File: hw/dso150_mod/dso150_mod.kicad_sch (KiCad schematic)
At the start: 23 parts, among them J1 USB_C_Receptacle_USB2.0, J2 Conn_01x02, J3 Conn_01x02, J4 Conn_01x04, J5 Conn_01x02, J6 Conn_01x01, SW1 SW_SPDT, U1 AP3012, U2 MCP73832-2-OT

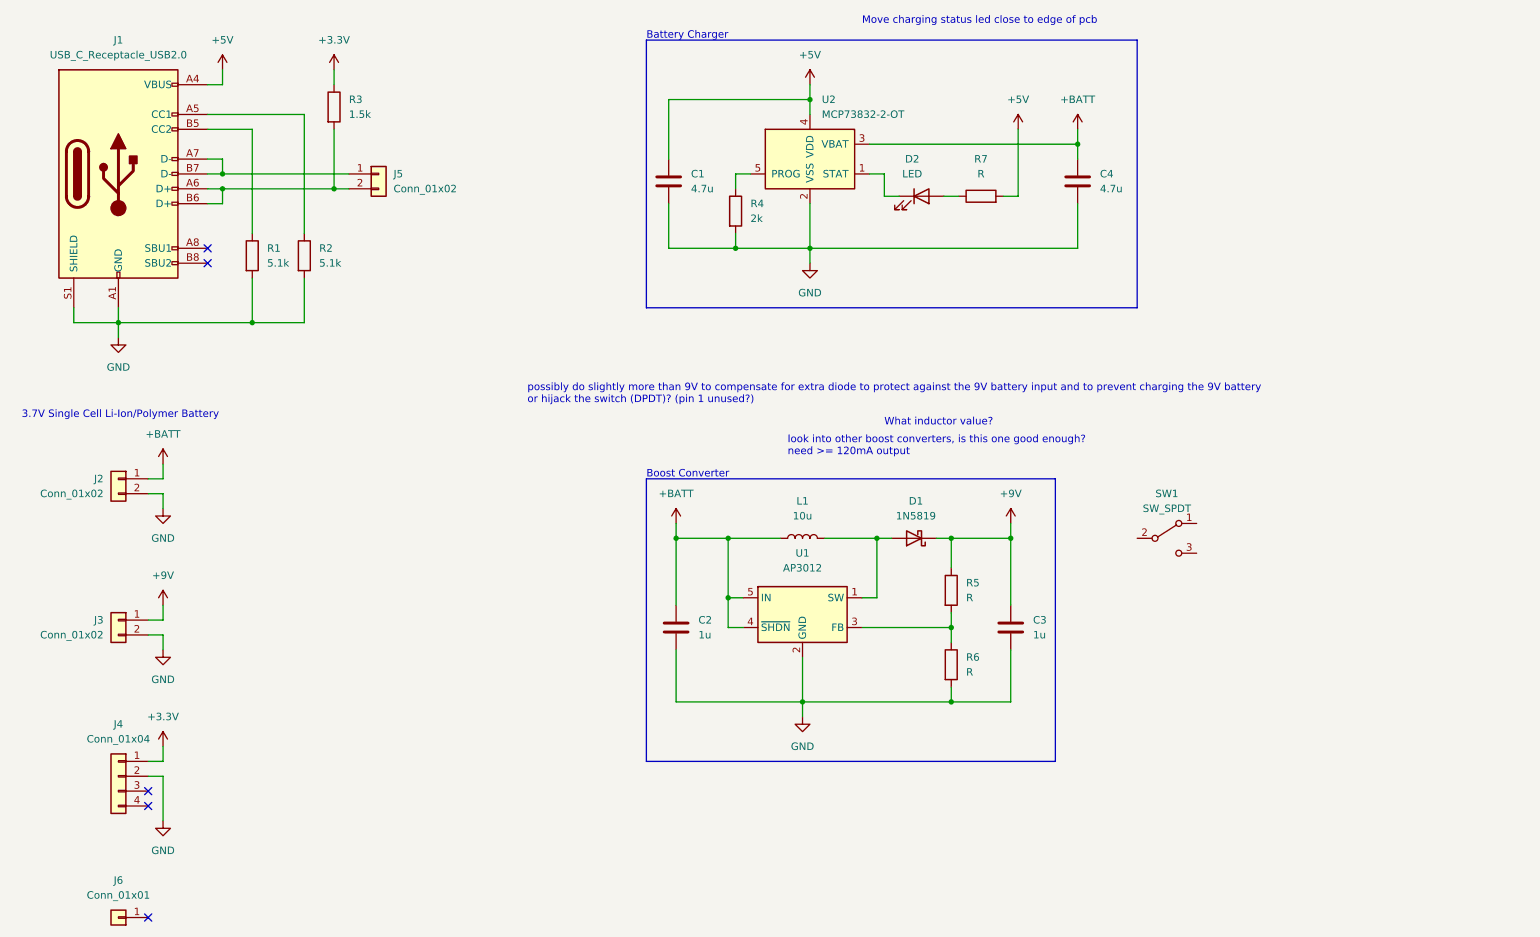
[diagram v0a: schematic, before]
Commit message: More layout placement, start traces
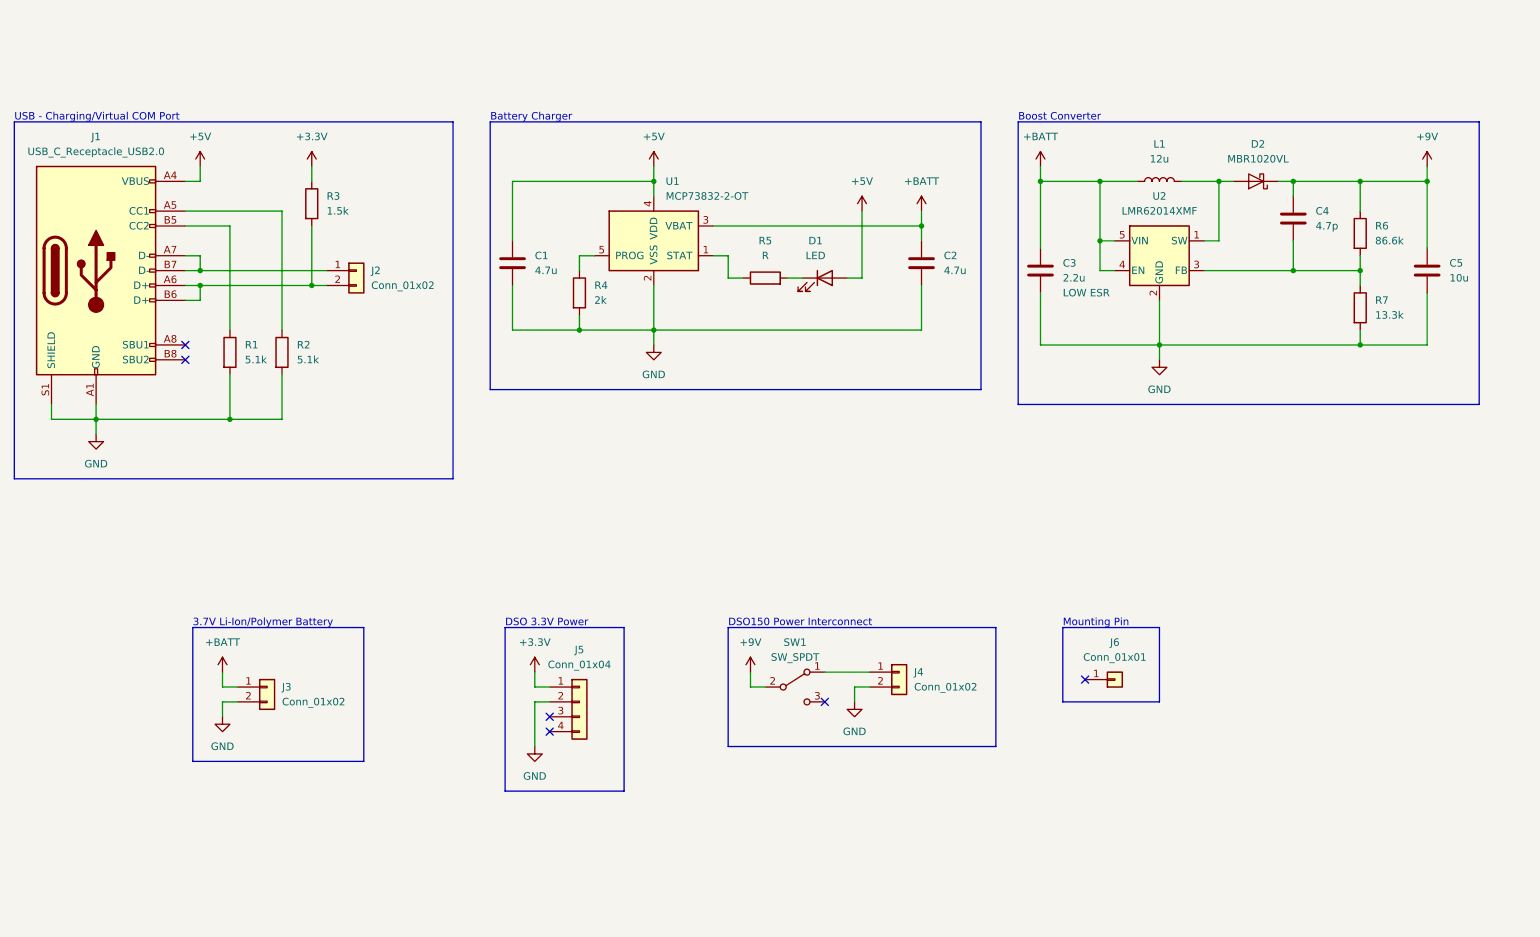
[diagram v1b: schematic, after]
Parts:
- removed D1: 1N5819, Diode_SMD:D_SOD-123F, symbol Device:D_Schottky
- removed U1: AP3012, Package_TO_SOT_SMD:SOT-23-5, symbol Regulator_Switching:AP3012
- added C4: 4.7p, Capacitor_SMD:C_0603_1608Metric, symbol Device:C
- added D2: MBR1020VL, Diode_SMD:D_SOD-123F, symbol Diode:MBR1020VL
- added U2: LMR62014XMF, Package_TO_SOT_SMD:SOT-23-5, symbol Regulator_Switching:LMR62014XMF
- C3: renamed from C2; value 1u -> 2.2u; Note (none) -> LOW ESR
- C5: renamed from C3; value 1u -> 10u
- L1: value 10u -> 12u; footprint Inductor_SMD:L_Bourns_SRN6045TA -> dso150_mod:L_Bourns_SRR0745A
- R6: renamed from R5; value R -> 86.6k
- R7: renamed from R6; value R -> 13.3k
- renumbered C4 to C2, D2 to D1, J5 to J2, J2 to J3, J3 to J4, J4 to J5, R7 to R5, U2 to U1
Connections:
- net +5V: now also D1.2 (A); no longer R5.2
- net +9V: now also SW1.2 (B), C4.1, D2.1 (K); no longer J4.1 (Pin_1)
- net +BATT: now also U2.4 (EN), U2.5 (VIN)
- net GND: now also U2.2 (GND)
- net at L1.2: now also D2.2 (A), U2.1 (SW)
- net at R6.2, R7.1: now also C4.2, U2.3 (FB)
- net at R5.1: now also U1.1 (STAT); no longer D1.2 (A)
- net at SW1.1 (A): now also J4.1 (Pin_1)
- net at D1.1 (K): now also R5.2; no longer U1.1 (STAT)
- no-connect marks 5 -> 6
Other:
- note added: "3.7V Li-Ion/Polymer Battery"
- note added: "DSO 3.3V Power"
- note added: "DSO150 Power Interconnect"
- note added: "Mounting Pin"
- note added: "USB - Charging/Virtual COM Port"
- note removed: "3.7V Single Cell Li-Ion/Polymer Battery"
- note removed: "Move charging status led close to edge of pcb"
- note removed: "What inductor value?"
- note removed: "look into other boost converters, is this one good enough? need >= 120mA output"
- note removed: "possibly do slightly more than 9V to compensate for extra diode to protect against the 9V battery input and to prevent charging the 9V battery or hijack the switch (DPDT)? (pin 1 unused?)"
- moved on the sheet: C1, C2, C3, C5, D1, J1, J2, J3, J4, J5, J6, L1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

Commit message: Disable boost converter to conserve battery, first final layout complete
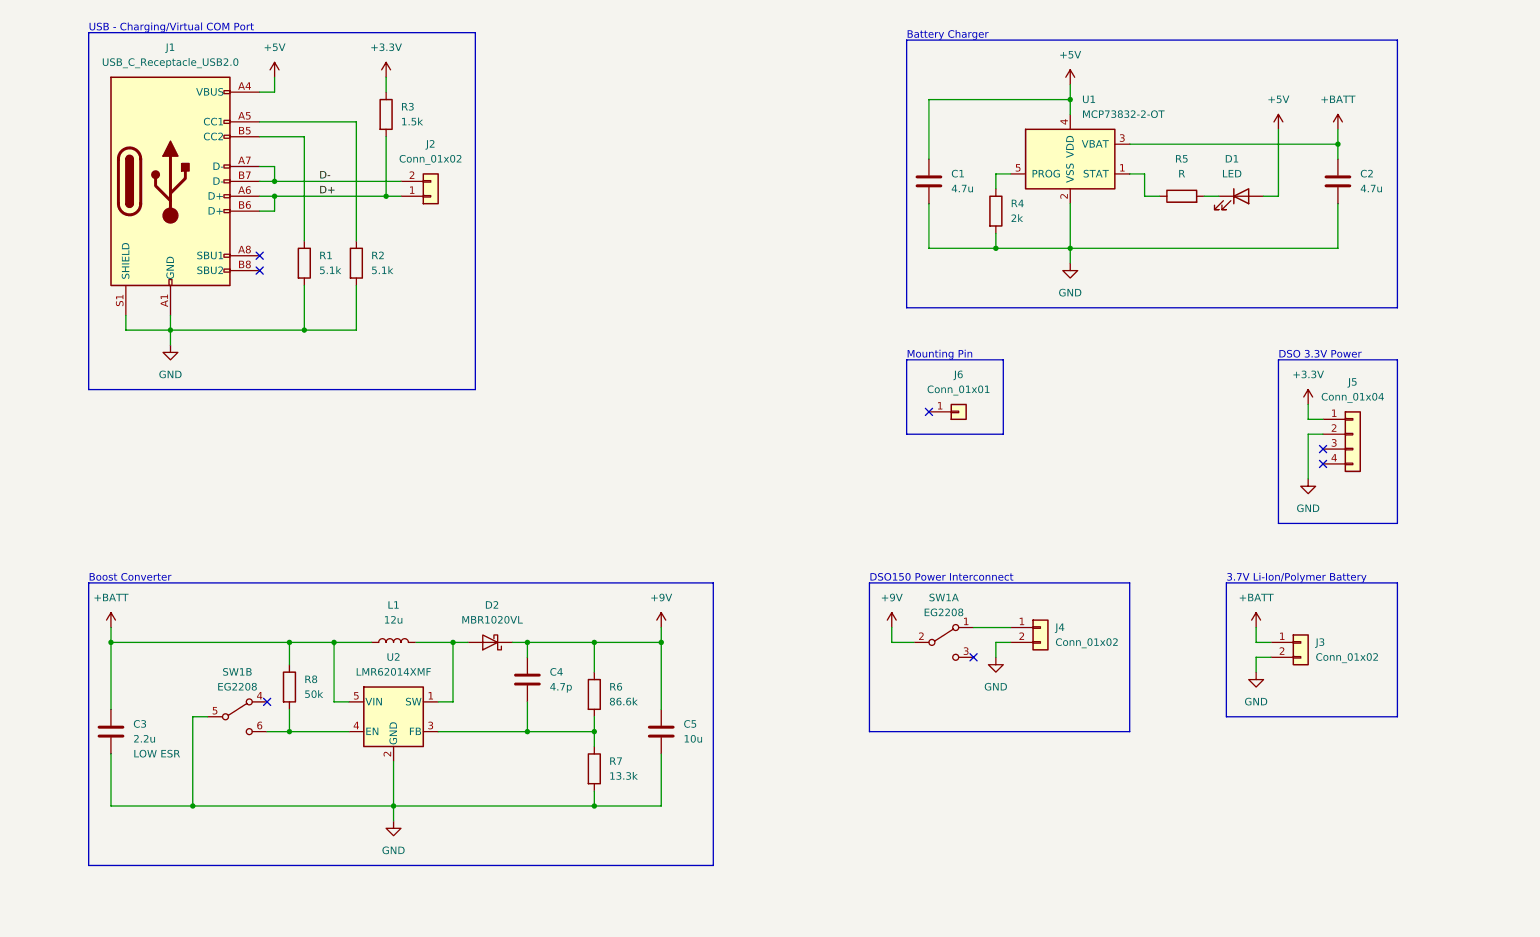
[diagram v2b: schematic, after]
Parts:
- removed SW1: SW_SPDT, Button_Switch_THT:SW_E-Switch_EG1224_SPDT_Angled, symbol Switch:SW_SPDT
- added R8: 50k, Resistor_SMD:R_0603_1608Metric, symbol Device:R
- added SW1: EG2208, dso150_mod:SW_E-Switch_EG2208_DPDT_Angled, symbol Switch:SW_DPDT_x2
- J1: footprint Connector_USB:USB_C_Receptacle_GCT_USB4085 -> dso150_mod:USB_C_Receptacle_GCT_USB4085
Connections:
- net +9V: now also SW1.2 (B)
- net +BATT: now also R8.1; no longer U2.4 (EN)
- net GND: now also SW1.5 (B)
- net D+: now reaches J1.A6 (D+), J1.B6 (D+), R3.2
- net D+: now also J2.1 (Pin_1); no longer J2.2 (Pin_2)
- net D-: now reaches J1.A7 (D-), J1.B7 (D-)
- net D-: now also J2.2 (Pin_2); no longer J2.1 (Pin_1)
- net at J4.1 (Pin_1): now also SW1.1 (A)
- new net: R8.2, SW1.6 (C), U2.4 (EN)
- no-connect marks 6 -> 7
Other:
- moved on the sheet: C1, C2, C3, C4, C5, D1, D2, J1, J2, J3, J4, J5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

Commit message: Add gerbers
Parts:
- C4: value 4.7p -> 470p
- D1: value LED -> LTST-C190KFKT
- L1: MPN (none) -> SRR0745A-120M
- R5: value R -> 150
- R8: value 50k -> 51k
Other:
- moved on the sheet: C1, D1, J4, J6, R4, R5, SW1A, U1
